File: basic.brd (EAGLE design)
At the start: 70.8 x 50.2 mm, 27 parts, among them U1 RASPBERRY_PICOTH

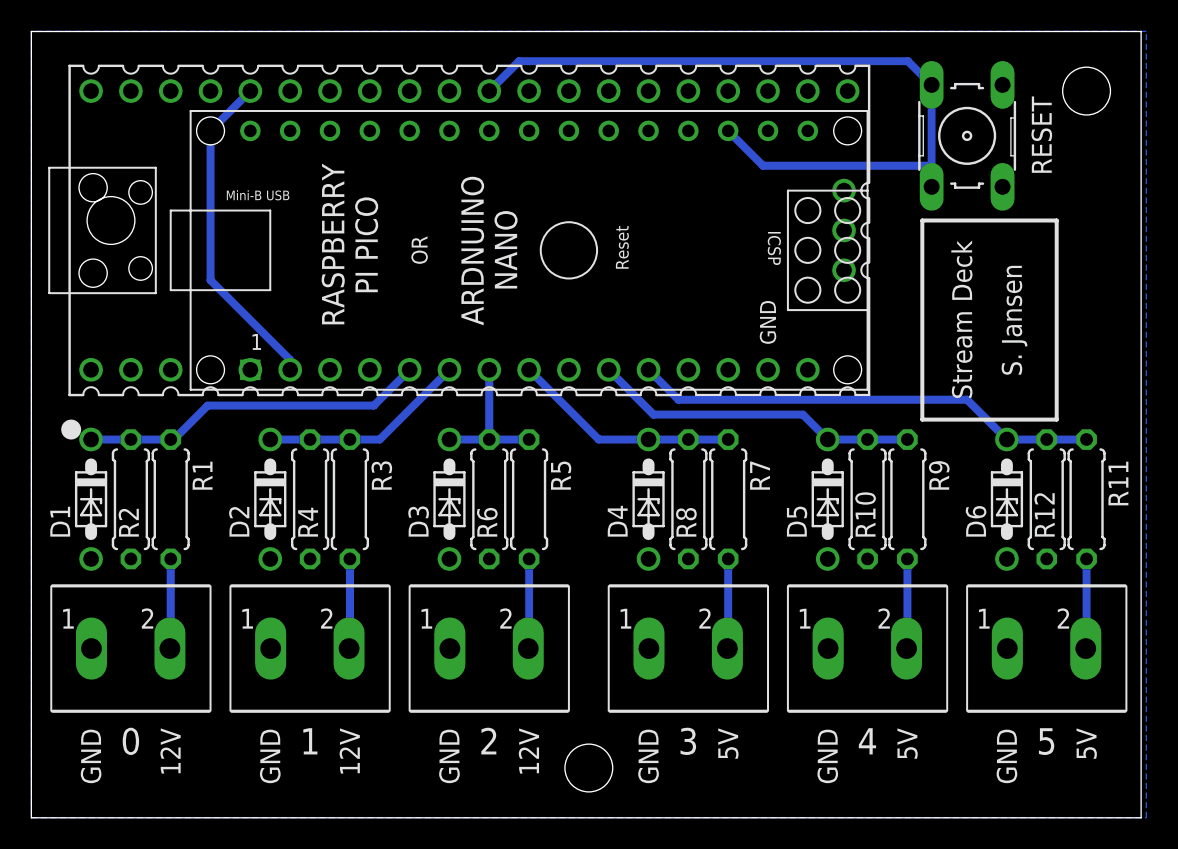
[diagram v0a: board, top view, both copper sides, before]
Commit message: Added capacitors to catch voltage spikes
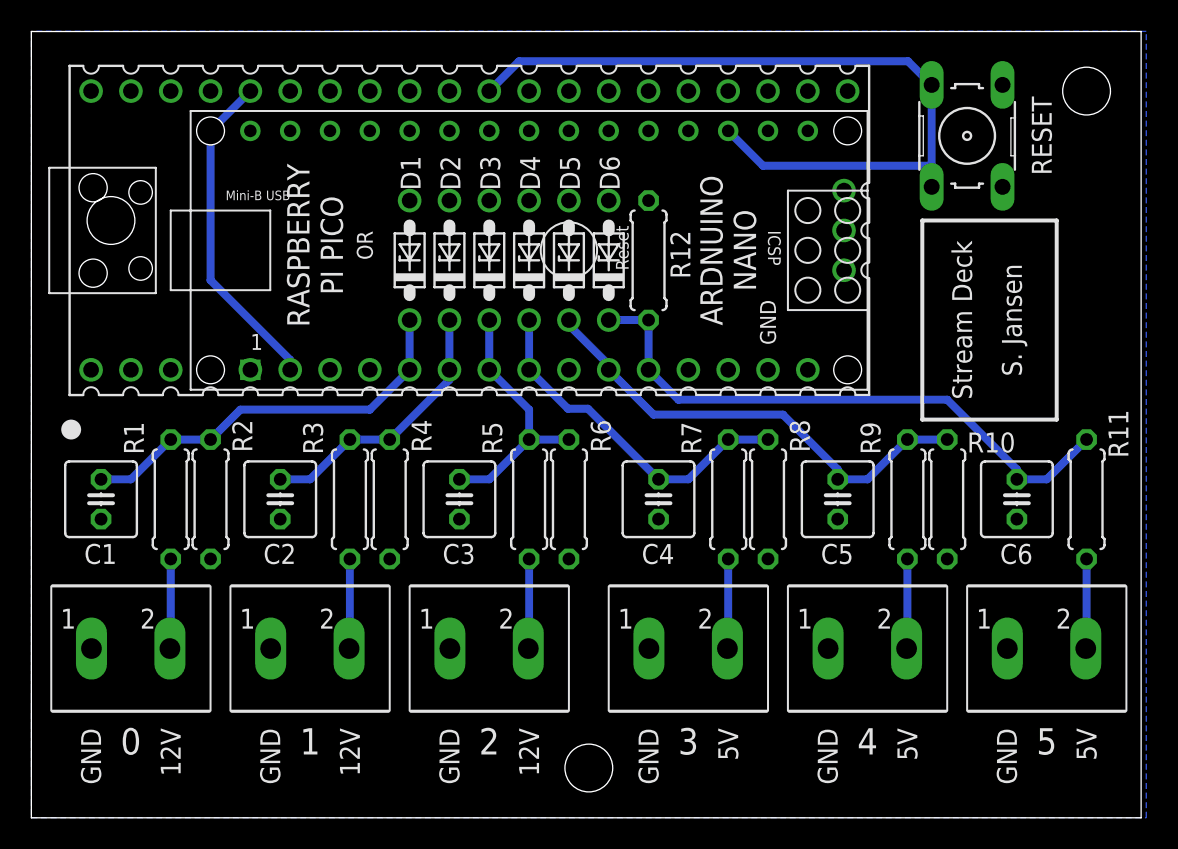
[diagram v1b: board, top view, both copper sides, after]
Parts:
- added C1, C2, C3, C4, C5, C6: (no value), rcl:C025-050X050
- moved D6 29.6 mm to (36.8, 35.6), turned to 90 degrees
- moved R12 29.6 mm to (39.4, 35.6), turned to 270 degrees
- moved D1 25.4 mm to (24.1, 35.6), turned to 90 degrees
- moved D5 22.5 mm to (34.3, 35.6), turned to 90 degrees
- moved D2 19.1 mm to (26.7, 35.6), turned to 90 degrees
- moved D4 17.0 mm to (31.8, 35.6), turned to 90 degrees
- moved D3 15.5 mm to (29.2, 35.6), turned to 90 degrees
- moved R8 5.08 mm to (47.0, 20.3)
- moved R2 5.08 mm to (11.4, 20.3)
- moved R10 5.08 mm to (58.4, 20.3)
- moved R4 5.08 mm to (22.9, 20.3)
- moved R6 5.08 mm to (34.3, 20.3)
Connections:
- net GND: now also C1.2, C2.2, C3.2, C4.2, C5.2, C6.2
- net PIN0: now also C1.1
- net PIN1: now also C2.1
- net PIN2: now also C3.1
- net PIN3: now also C4.1
- net PIN4: now also C5.1
- net PIN5: now also C6.1
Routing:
- net PIN4: track 20.9 -> 30.1 mm
- net PIN5: track 29.8 -> 38.0 mm
- net PIN3: track 14.5 -> 22.4 mm
- net PIN2: track 9.52 -> 16.7 mm
- net PIN1: track 13.3 -> 17.2 mm
- net PIN0: track 22.2 -> 25.9 mm
